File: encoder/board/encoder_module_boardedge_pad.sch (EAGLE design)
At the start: 5 parts

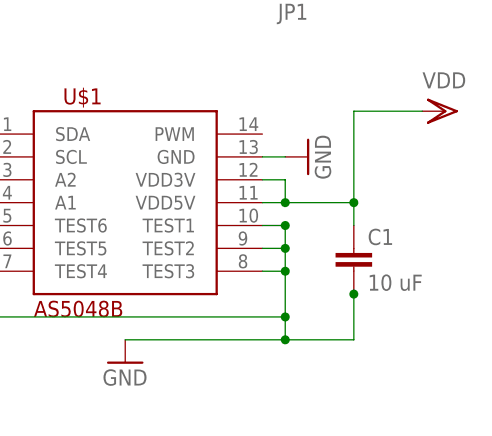
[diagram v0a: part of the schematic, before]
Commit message: Fixing small things preparing for panelization
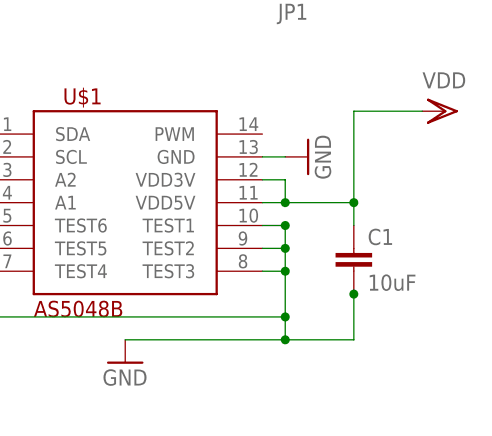
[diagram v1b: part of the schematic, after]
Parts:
- C1: value 10 uF -> 10uF
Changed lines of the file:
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@@
 <grid distance="0.1" unitdist="inch" unit="inch" style="lines" multiple="1" display="no" altdistance="0.01" altunitdist="inch" altunit="inch"/>
 <layers>
-<layer number="1" name="Top" color="4" fill="1" visible="yes" active="no"/>
-<layer number="2" name="Route2" color="1" fill="3" visible="yes" active="no"/>
-<layer number="3" name="Route3" color="4" fill="3" visible="yes" active="no"/>
-<layer number="4" name="Route4" color="1" fill="4" visible="yes" active="no"/>
-<layer number="5" name="Route5" color="4" fill="4" visible="yes" active="no"/>
-<layer number="6" name="Route6" color="1" fill="8" visible="yes" active="no"/>
-<layer number="7" name="Route7" color="4" fill="8" visible="yes" active="no"/>
-<layer number="8" name="Route8" color="1" fill="2" visible="yes" active="no"/>
-<layer number="9" name="Route9" color="4" fill="2" visible="yes" active="no"/>
-<layer number="10" name="Route10" color="1" fill="7" visible="yes" active="no"/>
-<layer number="11" name="Route11" color="4" fill="7" visible="yes" active="no"/>
-<layer number="12" name="Route12" color="1" fill="5" visible="yes" active="no"/>
-<layer number="13" name="Route13" color="4" fill="5" visible="yes" active="no"/>
-<layer number="14" name="Route14" color="1" fill="6" visible="yes" active="no"/>
-<layer number="15" name="Route15" color="4" fill="6" visible="yes" active="no"/>
-<layer number="16" name="Bottom" color="1" fill="1" visible="yes" active="no"/>
-<layer number="17" name="Pads" color="2" fill="1" visible="yes" active="no"/>
-<layer number="18" name="Vias" color="2" fill="1" visible="yes" active="no"/>
-<layer number="19" name="Unrouted" color="1" fill="1" visible="yes" active="no"/>
-<layer number="20" name="Dimension" color="15" fill="1" visible="yes" active="no"/>
-<layer number="21" name="tPlace" color="15" fill="1" visible="yes" active="no"/>
-<layer number="22" name="bPlace" color="7" fill="1" visible="yes" active="no"/>
-<layer number="23" name="tOrigins" color="15" fill="1" visible="yes" active="no"/>
-<layer number="24" name="bOrigins" color="15" fill="1" visible="yes" active="no"/>
-<layer number="25" name="tNames" color="7" fill="1" visible="yes" active="no"/>
-<layer number="26" name="bNames" color="7" fill="1" visible="yes" active="no"/>
-<layer number="27" name="tValues" color="7" fill="1" visible="yes" active="no"/>
-<layer number="28" name="bValues" color="7" fill="1" visible="yes" active="no"/>
+<layer number="1" name="Top" color="4" fill="1" visible="no" active="no"/>
+<layer number="2" name="Route2" color="1" fill="3" visible="no" active="no"/>
+<layer number="3" name="Route3" color="4" fill="3" visible="no" active="no"/>
+<layer number="4" name="Route4" color="1" fill="4" visible="no" active="no"/>
+<layer number="5" name="Route5" color="4" fill="4" visible="no" active="no"/>
+<layer number="6" name="Route6" color="1" fill="8" visible="no" active="no"/>
+<layer number="7" name="Route7" color="4" fill="8" visible="no" active="no"/>
+<layer number="8" name="Route8" color="1" fill="2" visible="no" active="no"/>
+<layer number="9" name="Route9" color="4" fill="2" visible="no" active="no"/>
+<layer number="10" name="Route10" color="1" fill="7" visible="no" active="no"/>
+<layer number="11" name="Route11" color="4" fill="7" visible="no" active="no"/>
+<layer number="12" name="Route12" color="1" fill="5" visible="no" active="no"/>
+<layer number="13" name="Route13" color="4" fill="5" visible="no" active="no"/>
+<layer number="14" name="Route14" color="1" fill="6" visible="no" active="no"/>
+<layer number="15" name="Route15" color="4" fill="6" visible="no" active="no"/>
+<layer number="16" name="Bottom" color="1" fill="1" visible="no" active="no"/>
+<layer number="17" name="Pads" color="2" fill="1" visible="no" active="no"/>
+<layer number="18" name="Vias" color="2" fill="1" visible="no" active="no"/>
+<layer number="19" name="Unrouted" color="1" fill="1" visible="no" active="no"/>
+<layer number="20" name="Dimension" color="15" fill="1" visible="no" active="no"/>
+<layer number="21" name="tPlace" color="15" fill="1" visible="no" active="no"/>
+<layer number="22" name="bPlace" color="7" fill="1" visible="no" active="no"/>
+<layer number="23" name="tOrigins" color="15" fill="1" visible="no" active="no"/>
+<layer number="24" name="bOrigins" color="15" fill="1" visible="no" active="no"/>
+<layer number="25" name="tNames" color="7" fill="1" visible="no" active="no"/>
+<layer number="26" name="bNames" color="7" fill="1" visible="no" active="no"/>
+<layer number="27" name="tValues" color="7" fill="1" visible="no" active="no"/>
+<layer number="28" name="bValues" color="7" fill="1" visible="no" active="no"/>
 <layer number="29" name="tStop" color="7" fill="3" visible="no" active="no"/>
 <layer number="30" name="bStop" color="7" fill="6" visible="no" active="no"/>
@@
 <layer number="35" name="tGlue" color="7" fill="4" visible="no" active="no"/>
 <layer number="36" name="bGlue" color="7" fill="5" visible="no" active="no"/>
-<layer number="37" name="tTest" color="7" fill="1" visible="yes" active="no"/>
-<layer number="38" name="bTest" color="7" fill="1" visible="yes" active="no"/>
+<layer number="37" name="tTest" color="7" fill="1" visible="no" active="no"/>
+<layer number="38" name="bTest" color="7" fill="1" visible="no" active="no"/>
 <layer number="39" name="tKeepout" color="4" fill="11" visible="no" active="no"/>
 <layer number="40" name="bKeepout" color="1" fill="11" visible="no" active="no"/>
@@
 <layer number="44" name="Drills" color="7" fill="1" visible="no" active="no"/>
 <layer number="45" name="Holes" color="7" fill="1" visible="no" active="no"/>
-<layer number="46" name="Milling" color="3" fill="1" visible="yes" active="no"/>
-<layer number="47" name="Measures" color="7" fill="1" visible="yes" active="no"/>
-<layer number="48" name="Document" color="7" fill="1" visible="yes" active="no"/>
-<layer number="49" name="Reference" color="7" fill="1" visible="yes" active="no"/>
-<layer number="50" name="dxf" color="7" fill="1" visible="yes" active="no"/>
-<layer number="51" name="tDocu" color="14" fill="1" visible="yes" active="no"/>
-<layer number="52" name="bDocu" color="7" fill="1" visible="yes" active="no"/>
-<layer number="53" name="tGND_GNDA" color="7" fill="9" visible="yes" active="no"/>
-<layer number="54" name="bGND_GNDA" color="1" fill="9" visible="yes" active="no"/>
-<layer number="56" name="wert" color="7" fill="1" visible="yes" active="no"/>
+<layer number="46" name="Milling" color="3" fill="1" visible="no" active="no"/>
+<layer number="47" name="Measures" color="7" fill="1" visible="no" active="no"/>
+<layer number="48" name="Document" color="7" fill="1" visible="no" active="no"/>
+<layer number="49" name="Reference" color="7" fill="1" visible="no" active="no"/>
+<layer number="50" name="dxf" color="7" fill="1" visible="no" active="no"/>
+<layer number="51" name="tDocu" color="14" fill="1" visible="no" active="no"/>
+<layer number="52" name="bDocu" color="7" fill="1" visible="no" active="no"/>
+<layer number="53" name="tGND_GNDA" color="7" fill="9" visible="no" active="no"/>
+<layer number="54" name="bGND_GNDA" color="1" fill="9" visible="no" active="no"/>
+<layer number="56" name="wert" color="7" fill="1" visible="no" active="no"/>
 <layer number="91" name="Nets" color="2" fill="1" visible="yes" active="yes"/>
 <layer number="92" name="Busses" color="1" fill="1" visible="yes" active="yes"/>
@@
 <part name="GND1" library="supply1" deviceset="GND" device=""/>
 <part name="VDD1" library="supply1" deviceset="VDD" device=""/>
-<part name="C1" library="SparkFun" deviceset="CAP" device="0603-CAP" value="10 uF"/>
+<part name="C1" library="SparkFun" deviceset="CAP" device="0603-CAP" value="10uF"/>
 <part name="GND2" library="supply1" deviceset="GND" device=""/>
 <part name="FRAME1" library="frames" deviceset="DINA3_L" device=""/>

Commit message: Board and component orders placed
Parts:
- C1: VOLTAGE (none) -> 6.3V
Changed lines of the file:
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@@
 <part name="GND1" library="supply1" deviceset="GND" device=""/>
 <part name="VDD1" library="supply1" deviceset="VDD" device=""/>
-<part name="C1" library="SparkFun" deviceset="CAP" device="0603-CAP" value="10uF"/>
+<part name="C1" library="SparkFun" deviceset="CAP" device="0603-CAP" value="10uF">
+<attribute name="VOLTAGE" value="6.3V"/>
+</part>
 <part name="GND2" library="supply1" deviceset="GND" device=""/>
 <part name="FRAME1" library="frames" deviceset="DINA3_L" device=""/>
@@
 <instance part="GND1" gate="1" x="20.32" y="25.4"/>
 <instance part="VDD1" gate="G$1" x="55.88" y="53.34" rot="R270"/>
-<instance part="C1" gate="G$1" x="45.72" y="35.56"/>
+<instance part="C1" gate="G$1" x="45.72" y="35.56">
+<attribute name="VOLTAGE" x="45.72" y="35.56" size="1.778" layer="96" display="off"/>
+</instance>
 <instance part="GND2" gate="1" x="40.64" y="48.26" rot="R90"/>
 <instance part="FRAME1" gate="G$1" x="-142.24" y="-99.06"/>
